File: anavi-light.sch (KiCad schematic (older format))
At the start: 13 parts, among them U1 CAT24C32WI-GT3

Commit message: ANAVI Light pHAT revision 1.0
Signed-off-by: Leon Anavi <leon@anavi.org>
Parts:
- added DC1: dc_jack, w_conn_misc:dc_socket, symbol dc_jack
- added PIR1: CONN_01X03, Pin_Headers:Pin_Header_Straight_1x03, symbol CONN_01X03
- added Q1, Q2, Q3: IRF8721PBF-1, SO-8, symbol IRF8721PBF-1
- added RGB1: Screw_Terminal_1x04, Terminal_Blocks:TerminalBlock_Pheonix_MKDS1.5-4pol, symbol Screw_Terminal_1x04
- JP1: symbol Jumper -> JUMPER
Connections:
- net +3V3: no longer C1.2, JP1.2, RASP_CONN1.14 (GND), RASP_CONN1.20 (GND), RASP_CONN1.25 (GND), RASP_CONN1.30 (GND), RASP_CONN1.34 (GND), RASP_CONN1.39 (GND), RASP_CONN1.6 (GND), RASP_CONN1.9 (GND), SENS1.2 (GND), SENS2.2 (GND), SENS3.2 (GND), U1.1 (A0), U1.2 (A1), U1.3 (A2), U1.4 (VSS), UART1.4 (P4)
- net +5V: now also PIR1.1 (P1)
- net at RASP_CONN1.19 (GPIO10/SPI_MOSI): now also Q1.4 (G)
- net at RASP_CONN1.21 (GPIO9/SPI_MISO): now also Q2.4 (G)
- net at RASP_CONN1.23 (GPIO11/SPI_SCLK): now also Q3.4 (G)
- net at RASP_CONN1.7 (GPIO4/GPCLK0): now also PIR1.2 (P2)
- new net: DC1.1, DC1.2, RGB1.1
- new net: Q3.5, Q3.6, Q3.7, Q3.8 (D), RGB1.2
- new net: Q2.5, Q2.6, Q2.7, Q2.8 (D), RGB1.3
- new net: Q1.5, Q1.6, Q1.7, Q1.8 (D), RGB1.4
- new net GND: C1.2, DC1.3, JP1.2, PIR1.3 (P3), Q1.1 (S), Q1.2, Q1.3, Q2.1 (S), Q2.2, Q2.3, Q3.1 (S), Q3.2, Q3.3, RASP_CONN1.14 (GND), RASP_CONN1.20 (GND), RASP_CONN1.25 (GND), RASP_CONN1.30 (GND), RASP_CONN1.34 (GND), RASP_CONN1.39 (GND), RASP_CONN1.6 (GND), RASP_CONN1.9 (GND), SENS1.2 (GND), SENS2.2 (GND), SENS3.2 (GND), U1.1 (A0), U1.2 (A1), U1.3 (A2), U1.4 (VSS), UART1.4 (P4)
- no-connect marks 21 -> 18

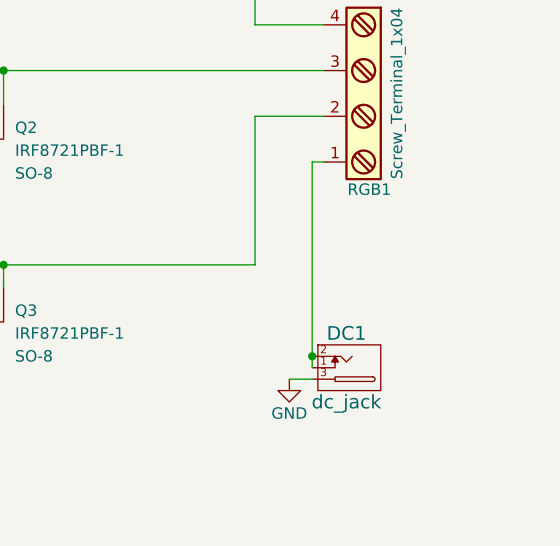
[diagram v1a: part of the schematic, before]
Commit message: anavi-light: Fixes
Suggested-by: Rangel Ivanov <rangelivanov88@gmail.com>
Signed-off-by: Leon Anavi <leon@anavi.org>
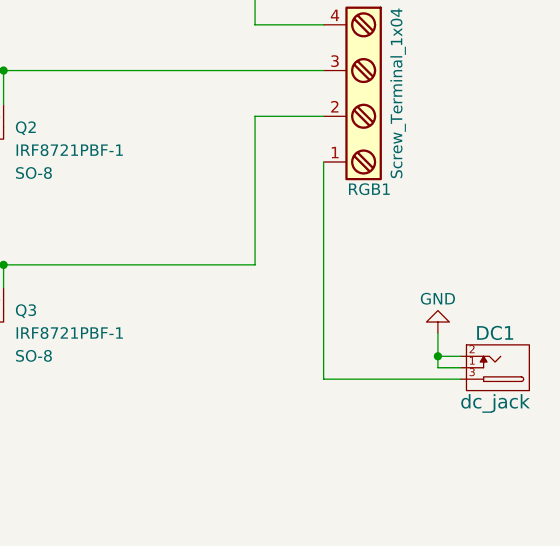
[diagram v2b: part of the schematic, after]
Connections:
- net GND: now also DC1.1, DC1.2; no longer DC1.3
- new net: DC1.3, RGB1.1
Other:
- moved on the sheet: DC1
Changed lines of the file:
@@
 L dc_jack DC1
 U 1 1 596E2E5E
-P 8450 4450
-F 0 "DC1" H 8450 4600 60  0000 C CNN
-F 1 "dc_jack" H 8450 4300 60  0000 C CNN
-F 2 "w_conn_misc:dc_socket" H 8450 4450 60  0001 C CNN
-F 3 "" H 8450 4450 60  0000 C CNN
-	1    8450 4450
+P 9100 4450
+F 0 "DC1" H 9100 4600 60  0000 C CNN
+F 1 "dc_jack" H 9100 4300 60  0000 C CNN
+F 2 "w_conn_misc:dc_socket" H 9100 4450 60  0001 C CNN
+F 3 "" H 9100 4450 60  0000 C CNN
+	1    9100 4450
 	1    0    0    -1
 $EndComp
@@
 Wire Wire Line
 	6200 4350 6350 4350
-Wire Wire Line
-	8300 3550 8300 4450
-Wire Wire Line
-	8300 3550 8350 3550
 $Comp
-L GND #PWR018
-U 1 1 596E275D
-P 8200 4500
-F 0 "#PWR018" H 8200 4250 50  0001 C CNN
-F 1 "GND" H 8200 4350 50  0000 C CNN
-F 2 "" H 8200 4500 50  0000 C CNN
-F 3 "" H 8200 4500 50  0000 C CNN
-	1    8200 4500
-	1    0    0    -1
+L GND #PWR?
+U 1 1 596F2E09
+P 8850 4300
+F 0 "#PWR?" H 8850 4050 50  0001 C CNN
+F 1 "GND" H 8850 4150 50  0000 C CNN
+F 2 "" H 8850 4300 50  0000 C CNN
+F 3 "" H 8850 4300 50  0000 C CNN
+	1    8850 4300
+	-1   0    0    1
 $EndComp
 Wire Wire Line
-	8300 4500 8200 4500
-Connection ~ 8300 4400
+	8950 4450 8850 4450
+Wire Wire Line
+	8850 4450 8850 4300
+Wire Wire Line
+	8950 4400 8850 4400
+Connection ~ 8850 4400
+Wire Wire Line
+	8350 3550 8350 4500
+Wire Wire Line
+	8350 4500 8950 4500
 $EndSCHEMATC

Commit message: Adjust labels on front silkscreen
Signed-off-by: Leon Anavi <leon@anavi.org>
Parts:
- renumbered R6 to R4, R7 to R5
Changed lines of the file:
@@
 $EndComp
 $Comp
-L R R6
+L R R4
 U 1 1 570C0762
 P 6200 900
-F 0 "R6" H 6150 750 50  0000 C CNN
+F 0 "R4" H 6150 750 50  0000 C CNN
 F 1 "4.7K" V 6200 900 50  0000 C CNN
 F 2 "Resistors_SMD:R_0603_HandSoldering" V 6130 900 50  0001 C CNN
@@
 $EndComp
 $Comp
-L R R7
+L R R5
 U 1 1 570C0BD5
 P 6350 900
-F 0 "R7" H 6450 750 50  0000 C CNN
+F 0 "R5" H 6450 750 50  0000 C CNN
 F 1 "4.7K" V 6350 900 50  0000 C CNN
 F 2 "Resistors_SMD:R_0603_HandSoldering" V 6280 900 50  0001 C CNN
@@
 	6200 4350 6350 4350
 $Comp
-L GND #PWR?
+L GND #PWR018
 U 1 1 596F2E09
 P 8850 4300
-F 0 "#PWR?" H 8850 4050 50  0001 C CNN
+F 0 "#PWR018" H 8850 4050 50  0001 C CNN
 F 1 "GND" H 8850 4150 50  0000 C CNN
 F 2 "" H 8850 4300 50  0000 C CNN

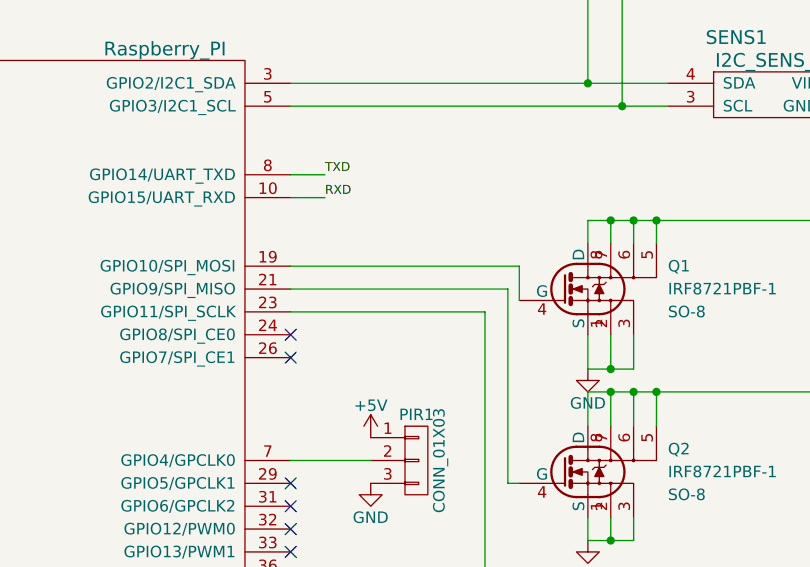
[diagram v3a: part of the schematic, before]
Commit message: Add MOSFET gate resistors
Signed-off-by: Leon Anavi <leon@anavi.org>
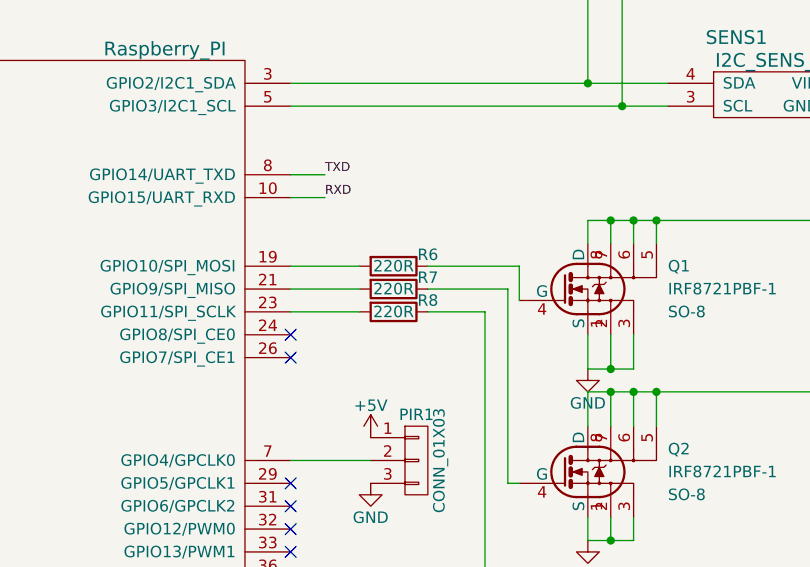
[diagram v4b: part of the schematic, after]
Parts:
- added R6, R7, R8: 220R, Resistors_SMD:R_0603_HandSoldering, symbol R
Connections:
- net at RASP_CONN1.19 (GPIO10/SPI_MOSI): now also R6.2; no longer Q1.4 (G)
- net at RASP_CONN1.21 (GPIO9/SPI_MISO): now also R7.2; no longer Q2.4 (G)
- net at RASP_CONN1.23 (GPIO11/SPI_SCLK): now also R8.2; no longer Q3.4 (G)
- new net: Q1.4 (G), R6.1
- new net: Q2.4 (G), R7.1
- new net: Q3.4 (G), R8.1
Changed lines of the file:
@@
 Connection ~ 6950 2400
 Wire Wire Line
-	5350 2600 6350 2600
-Wire Wire Line
 	6350 2600 6350 2750
-Wire Wire Line
-	5350 2700 6300 2700
 Wire Wire Line
 	6300 2700 6300 3550
 Wire Wire Line
 	6300 3550 6350 3550
-Wire Wire Line
-	5350 2800 6200 2800
 Wire Wire Line
 	6200 2800 6200 4350
@@
 Wire Wire Line
 	8350 4500 8950 4500
+$Comp
+L R R6
+U 1 1 5991FAAA
+P 5800 2600
+F 0 "R6" V 5750 2750 50  0000 C CNN
+F 1 "220R" V 5800 2600 50  0000 C CNN
+F 2 "Resistors_SMD:R_0603_HandSoldering" V 5730 2600 50  0001 C CNN
+F 3 "" H 5800 2600 50  0000 C CNN
+	1    5800 2600
+	0    1    1    0
+$EndComp
+Wire Wire Line
+	5950 2600 6350 2600
+Wire Wire Line
+	5650 2600 5350 2600
+$Comp
+L R R7
+U 1 1 5991FFC0
+P 5800 2700
+F 0 "R7" V 5750 2850 50  0000 C CNN
+F 1 "220R" V 5800 2700 50  0000 C CNN
+F 2 "Resistors_SMD:R_0603_HandSoldering" V 5730 2700 50  0001 C CNN
+F 3 "" H 5800 2700 50  0000 C CNN
+	1    5800 2700
+	0    1    1    0
+$EndComp
+Wire Wire Line
+	5950 2700 6300 2700
+Wire Wire Line
+	5650 2700 5350 2700
+$Comp
+L R R8
+U 1 1 5992025A
+P 5800 2800
+F 0 "R8" V 5750 2950 50  0000 C CNN
+F 1 "220R" V 5800 2800 50  0000 C CNN
+F 2 "Resistors_SMD:R_0603_HandSoldering" V 5730 2800 50  0001 C CNN
+F 3 "" H 5800 2800 50  0000 C CNN
+	1    5800 2800
+	0    1    1    0
+$EndComp
+Wire Wire Line
+	5950 2800 6200 2800
+Wire Wire Line
+	5650 2800 5350 2800
 $EndSCHEMATC
